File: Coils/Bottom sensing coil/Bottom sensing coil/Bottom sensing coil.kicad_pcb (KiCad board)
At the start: 2 copper layers, 74.8 x 56.5 mm, 7 parts, among them J1 Conn_01x02_Socket, J2 Conn_01x02_Pin

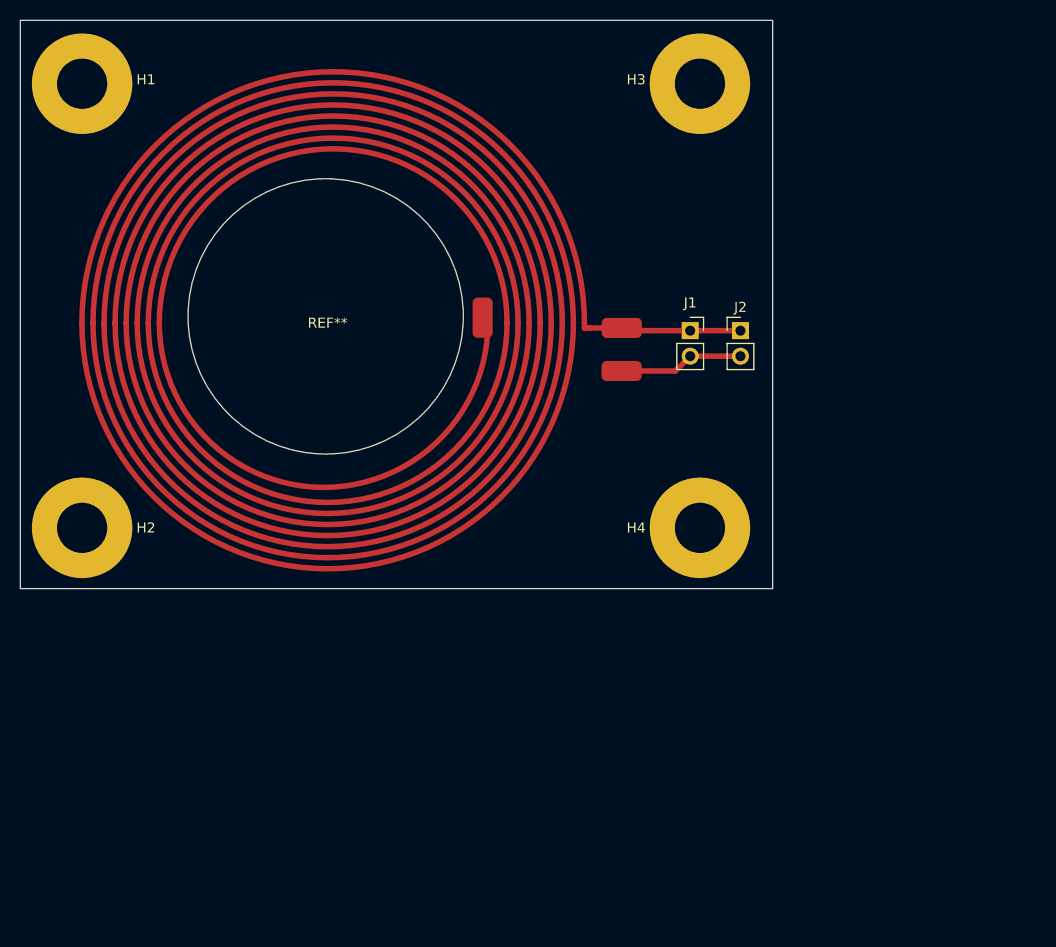
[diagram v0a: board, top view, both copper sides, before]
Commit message: added 3d models for OPA3692, THS3091 and BNC connector
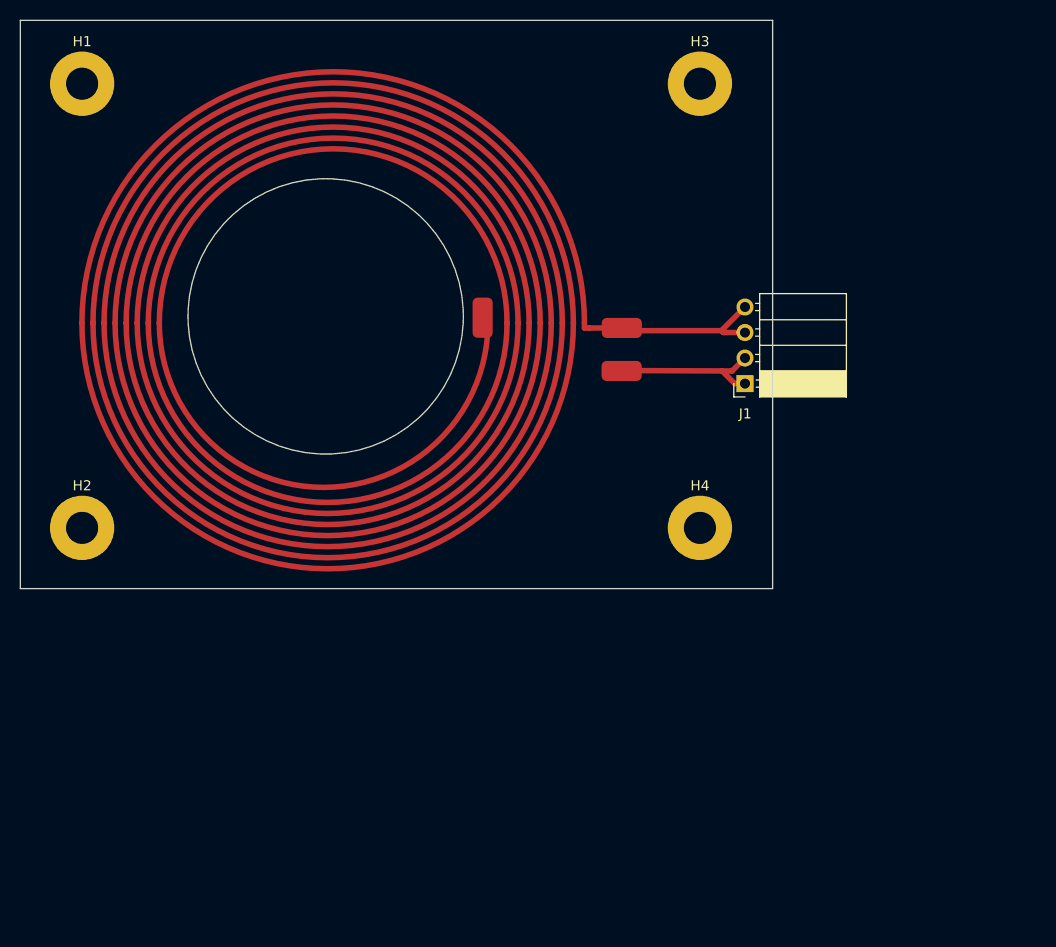
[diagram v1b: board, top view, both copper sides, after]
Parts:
- removed J2: Conn_01x02_Pin, Connector_PinHeader_2.54mm:PinHeader_1x02_P2.54mm_Vertical
- H1, H2, H3, H4: footprint MountingHole:MountingHole_5mm_Pad -> MountingHole:MountingHole_3.2mm_M3_Pad
- J1: value Conn_01x02_Socket -> Conn_01x04_Socket; footprint Connector_PinSocket_2.54mm:PinSocket_1x02_P2.54mm_Vertical -> Connector_PinSocket_2.54mm:PinSocket_1x04_P2.54mm_Horizontal
- moved J1 7.58 mm to (189.8, 101.2), turned to 180 degrees
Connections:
- J1 pad 1: /coil start -> /coil end
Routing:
- net /coil end: track 12.4 -> 15.7 mm
- net /coil start: track 12.7 -> 15.8 mm

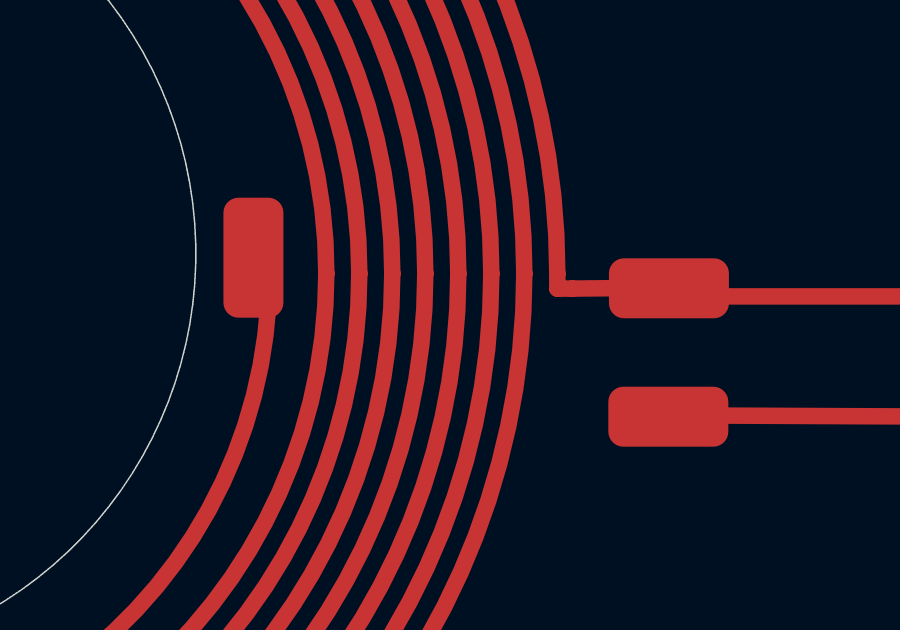
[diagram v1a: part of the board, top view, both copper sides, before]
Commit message: Small corrections, changed footprint for edge SMA connectors
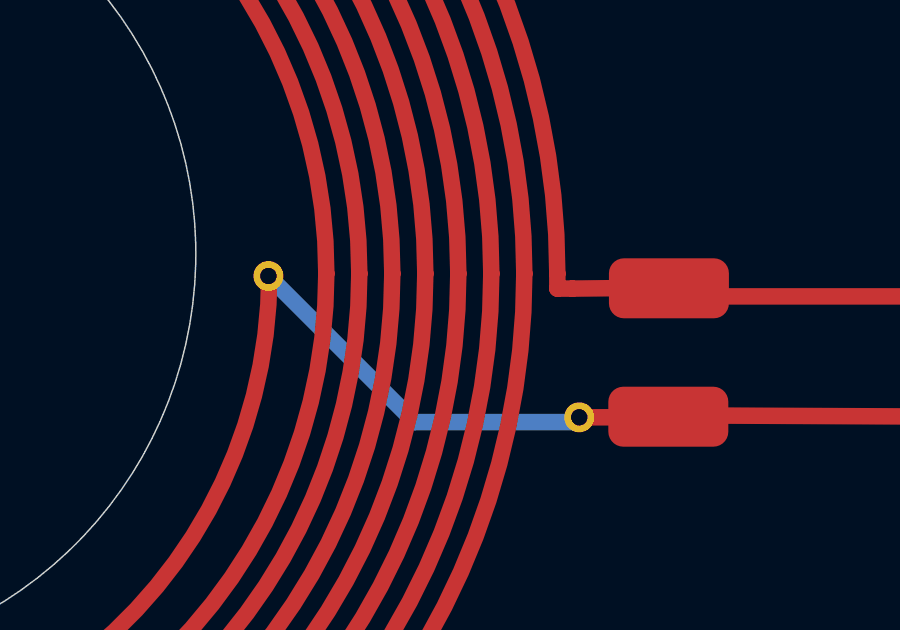
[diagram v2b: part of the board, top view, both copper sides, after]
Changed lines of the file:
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@@
+		)
+		(fp_line
+			(start 26.28 4.79)
+			(end 26.28 4.79)
+			(stroke
+				(width 0.55)
+				(type default)
+			)
+			(layer "F.Cu")
+		)
+		(fp_line
+			(start 26.28 4.79)
+			(end 29.25 4.79)
+			(stroke
+				(width 0.55)
+				(type default)
+			)
+			(layer "F.Cu")
 		)
 		(fp_line
@@
 			(layer "F.Cu")
 		)
-		(pad "" smd roundrect
-			(at 15.42 -0.53 270)
-			(size 4 2)
-			(layers "F.Cu")
-			(roundrect_rratio 0.25)
+		(fp_line
+			(start 15.92 0.08)
+			(end 20.79 4.95)
+			(stroke
+				(width 0.55)
+				(type default)
+			)
+			(layer "B.Cu")
+		)
+		(fp_line
+			(start 20.79 4.95)
+			(end 26.28 4.95)
+			(stroke
+				(width 0.55)
+				(type default)
+			)
+			(layer "B.Cu")
+		)
+		(fp_line
+			(start 26.28 4.79)
+			(end 26.28 4.79)
+			(stroke
+				(width 0.55)
+				(type default)
+			)
+			(layer "B.Cu")
+		)
+		(pad "" thru_hole circle
+			(at 15.92 0.08 270)
+			(size 1 1)
+			(drill 0.55)
+			(layers "*.Cu" "*.Mask")
+			(remove_unused_layers no)
+		)
+		(pad "" thru_hole circle
+			(at 26.28 4.79 270)
+			(size 1 1)
+			(drill 0.55)
+			(layers "*.Cu" "*.Mask")
+			(remove_unused_layers no)
 		)
 		(pad "1" smd roundrect

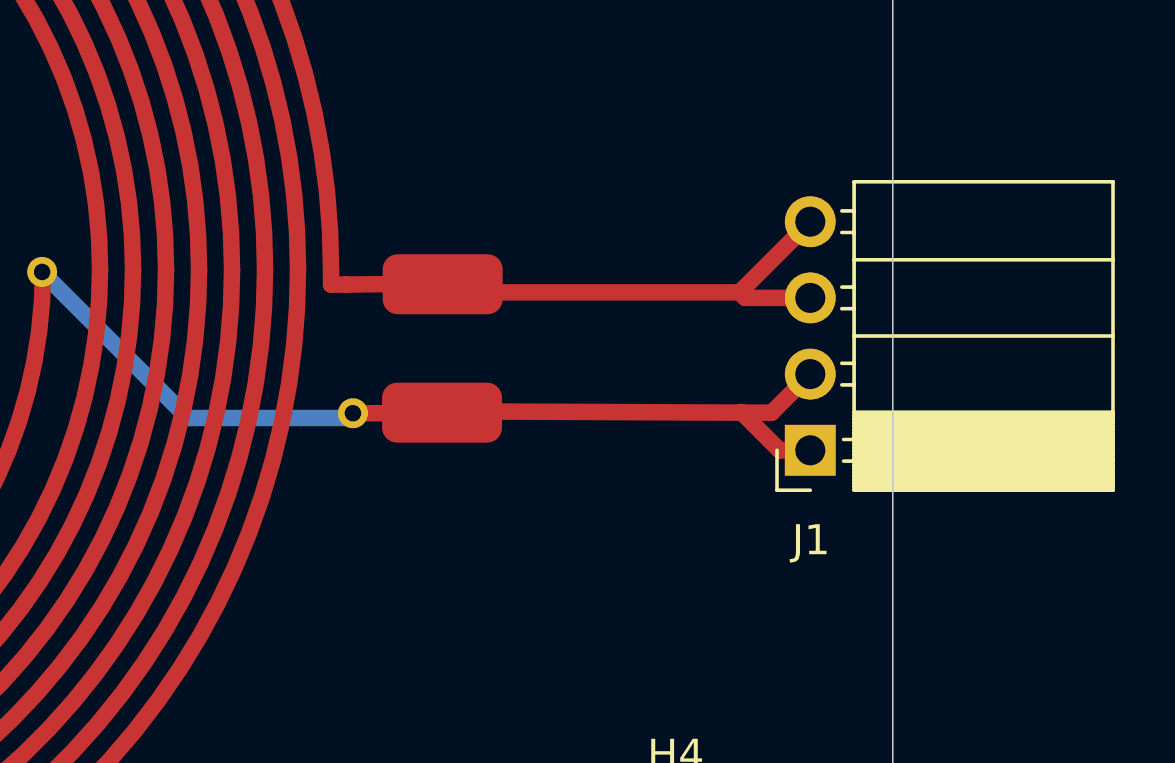
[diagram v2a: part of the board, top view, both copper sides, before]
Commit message: Added via stiching to TX board, moved almost all vias off of pads, increased the trace width for the power supply and changed coil connector to horizontal socket
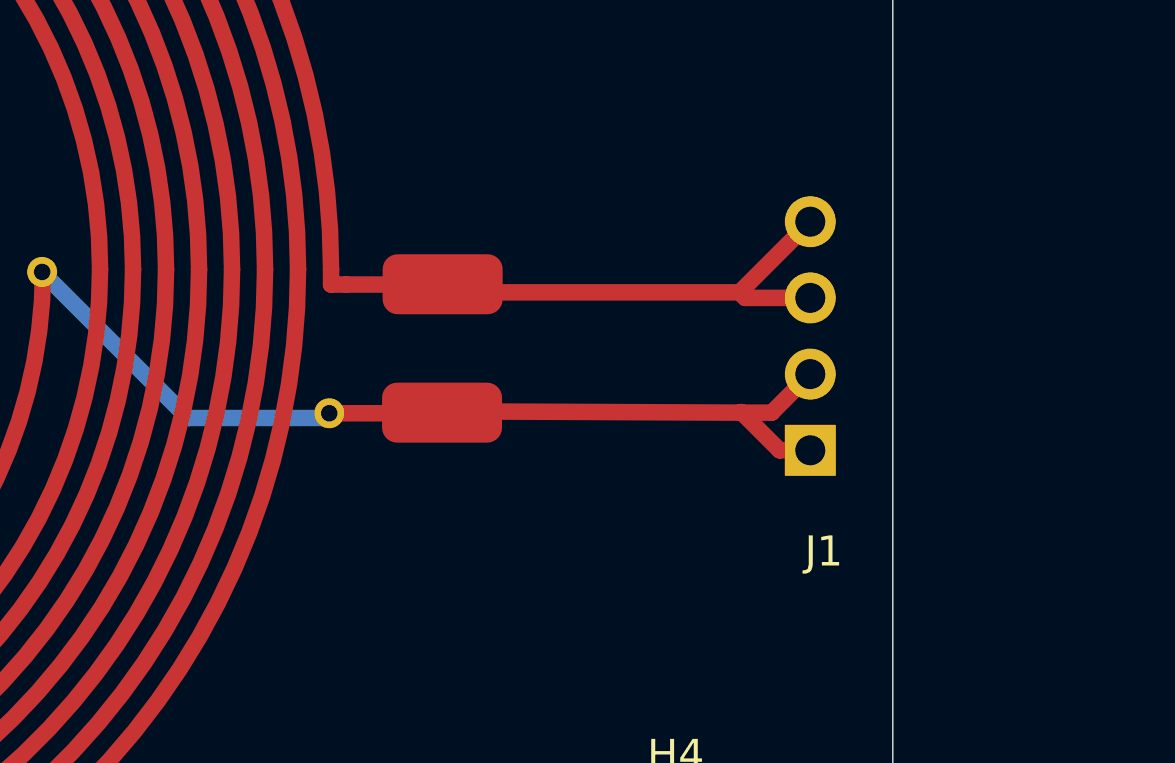
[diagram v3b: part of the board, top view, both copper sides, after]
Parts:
- J1: value Conn_01x04_Socket -> Conn_01x04; footprint Connector_PinSocket_2.54mm:PinSocket_1x04_P2.54mm_Horizontal -> Connector_PinHeader_2.54mm:PinHeader_1x04_P2.54mm_Horizontal; moved to B.Cu
- turned J1 to 0 degrees
